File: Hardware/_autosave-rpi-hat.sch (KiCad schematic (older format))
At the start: 2 parts, among them J1 Conn_02x20_Odd_Even__Rpi, J2 USART

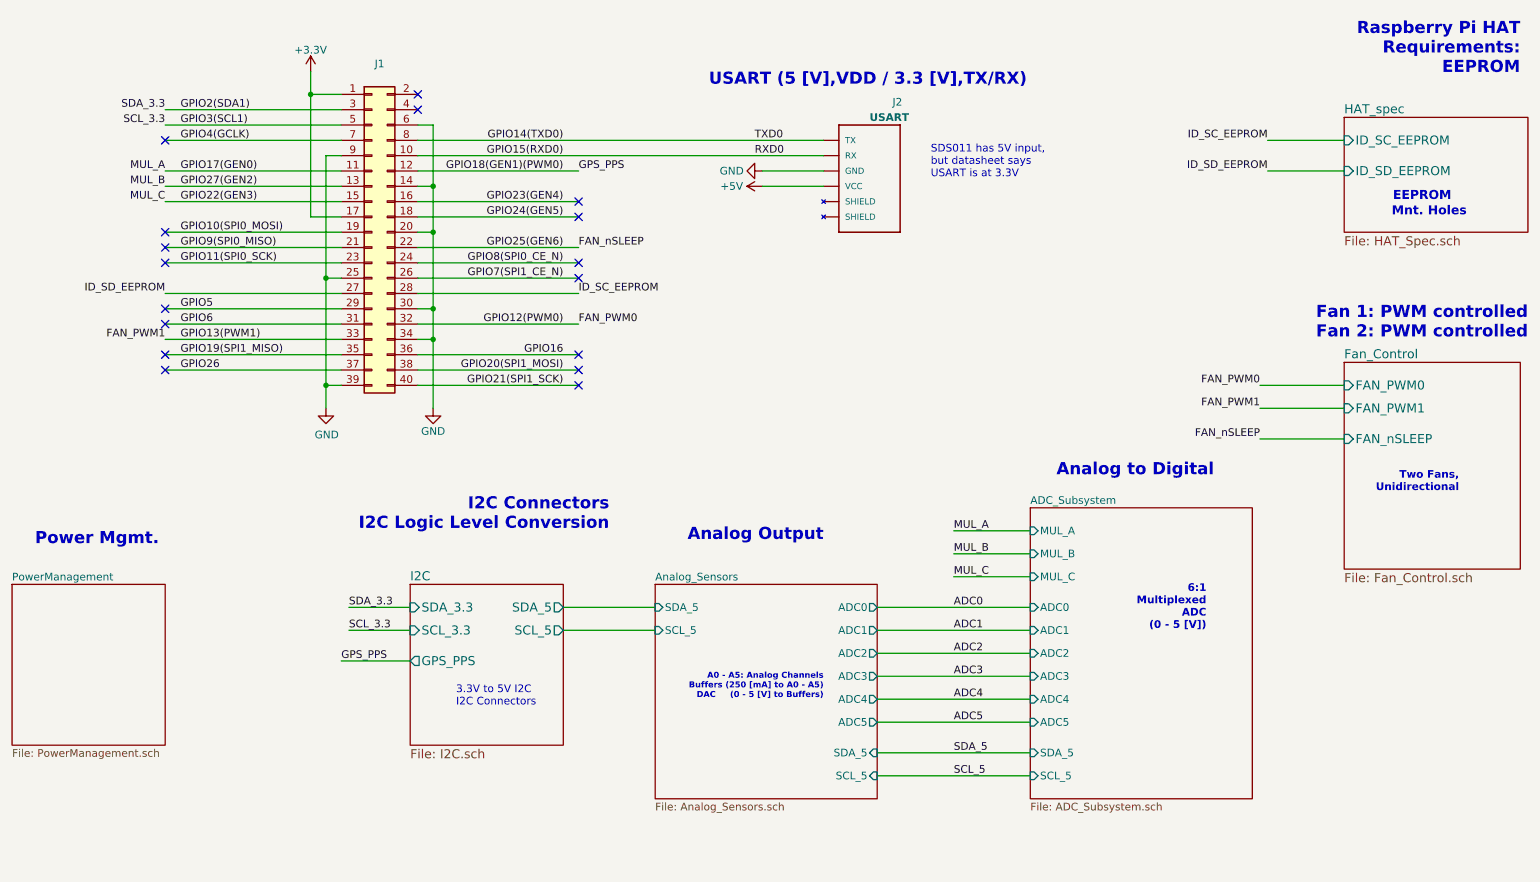
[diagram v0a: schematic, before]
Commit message: Organized Schematic Naming and Added Comments
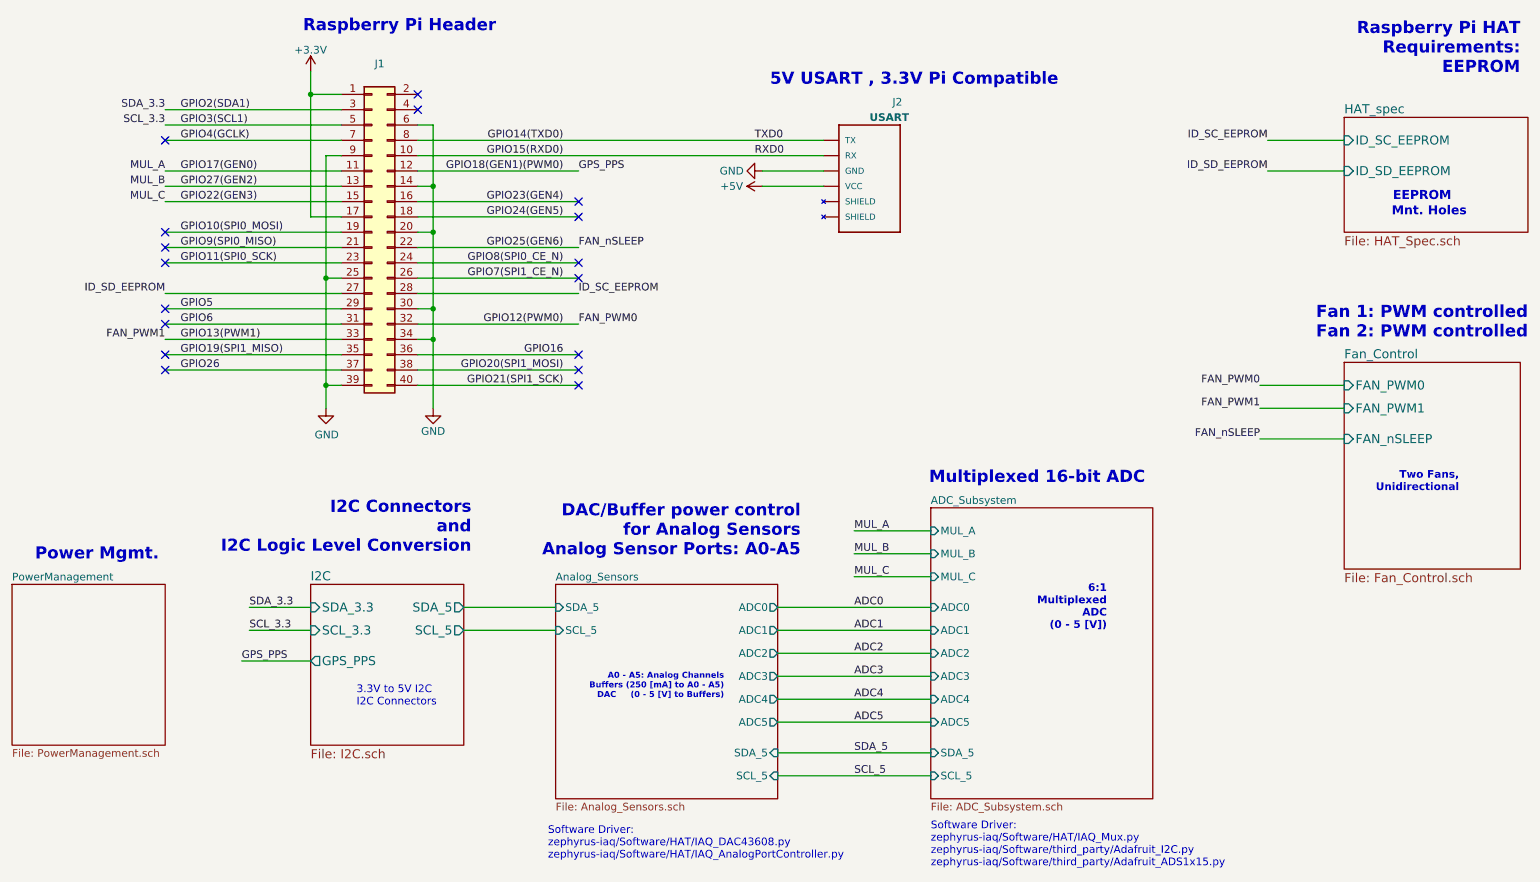
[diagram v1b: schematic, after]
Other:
- note added: "5V USART , 3.3V Pi Compatible"
- note added: "DAC/Buffer power control\n for Analog Sensors\nAnalog Sensor Ports: A0-A5\n\n"
- note added: "I2C Connectors\nand\nI2C Logic Level Conversion"
- note added: "Multiplexed 16-bit ADC"
- note added: "Raspberry Pi Header"
- note added: "Software Driver:\nzephyrus-iaq/Software/HAT/IAQ_DAC43608.py\nzephyrus-iaq/Software/HAT/IAQ_AnalogPortController.py"
- note added: "Software Driver:\nzephyrus-iaq/Software/HAT/IAQ_Mux.py\nzephyrus-iaq/Software/third_party/Adafruit_I2C.py\nzephyrus-iaq/Software/third_party/Adafruit_ADS1x15.py"
- note removed: "Analog Output\n\n"
- note removed: "Analog to Digital"
- note removed: "I2C Connectors\nI2C Logic Level Conversion"
- note removed: "SDS011 has 5V input, \nbut datasheet says \nUSART is at 3.3V"
- note removed: "USART (5 [V],VDD / 3.3 [V],TX/RX)"
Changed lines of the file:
@@
 EESchema Schematic File Version 4
-LIBS:rpi-hat-cache
 EELAYER 30 0
 EELAYER END
@@
 encoding utf-8
 Sheet 1 7
-Title ""
-Date "15 nov 2012"
+Title "IAQ HAT Top Level"
+Date "2019-11-15"
 Rev ""
-Comp ""
+Comp "Zephyrus, Indoor Air Quality - Raspberry Pi HAT"
 Comment1 ""
 Comment2 ""
@@
 	1    0    0    -1
 $EndComp
-Text Notes 5550 1150 0    79   ~ 16
-USART (5 [V],VDD / 3.3 [V],TX/RX)
-Text Label 7150 4550 0    50   ~ 0
+Text Notes 5950 1150 0    79   ~ 16
+5V USART , 3.3V Pi Compatible
+Text Label 6500 4550 0    50   ~ 0
 ADC0
-Text Label 7150 4700 0    50   ~ 0
+Text Label 6500 4700 0    50   ~ 0
 ADC1
-Text Label 7150 4850 0    50   ~ 0
+Text Label 6500 4850 0    50   ~ 0
 ADC2
-Text Label 7150 5000 0    50   ~ 0
+Text Label 6500 5000 0    50   ~ 0
 ADC3
-Text Label 7150 5150 0    50   ~ 0
+Text Label 6500 5150 0    50   ~ 0
 ADC4
-Text Label 7150 5300 0    50   ~ 0
+Text Label 6500 5300 0    50   ~ 0
 ADC5
-Text Label 3200 4550 0    50   ~ 0
+Text Label 2550 4550 0    50   ~ 0
 SDA_3.3
 Text Label 2000 1300 2    50   ~ 0
@@
 	3050 1600 3050 2400
 Connection ~ 3050 2400
-Text Notes 7000 1750 0    50   ~ 0
-SDS011 has 5V input, \nbut datasheet says \nUSART is at 3.3V
 NoConn ~ 4700 2300
 NoConn ~ 2000 2100
@@
 NoConn ~ 2000 2300
 $Sheet
-S 7650 3900 1450 1900
+S 7000 3900 1450 1900
 U 5D9BB3B6
 F0 "ADC_Subsystem" 50
 F1 "ADC_Subsystem.sch" 50
-F2 "ADC0" I L 7650 4550 50
-F3 "ADC1" I L 7650 4700 50
-F4 "ADC2" I L 7650 4850 50
-F5 "ADC3" I L 7650 5000 50
-F6 "ADC4" I L 7650 5150 50
-F7 "ADC5" I L 7650 5300 50
-F8 "MUL_A" I L 7650 4050 50
-F9 "MUL_B" I L 7650 4200 50
-F10 "MUL_C" I L 7650 4350 50
-F11 "SDA_5" I L 7650 5500 50
-F12 "SCL_5" I L 7650 5650 50
-$EndSheet
-Text Label 7150 4050 0    50   ~ 0
+F2 "ADC0" I L 7000 4550 50
+F3 "ADC1" I L 7000 4700 50
+F4 "ADC2" I L 7000 4850 50
+F5 "ADC3" I L 7000 5000 50
+F6 "ADC4" I L 7000 5150 50
+F7 "ADC5" I L 7000 5300 50
+F8 "MUL_A" I L 7000 4050 50
+F9 "MUL_B" I L 7000 4200 50
+F10 "MUL_C" I L 7000 4350 50
+F11 "SDA_5" I L 7000 5500 50
+F12 "SCL_5" I L 7000 5650 50
+$EndSheet
+Text Label 6500 4050 0    50   ~ 0
 MUL_A
 Wire Wire Line
-	7650 4050 7150 4050
-Wire Wire Line
-	7150 4200 7650 4200
-Wire Wire Line
-	7150 4350 7650 4350
-Text Label 7150 5500 0    50   ~ 0
+	7000 4050 6500 4050
+Wire Wire Line
+	6500 4200 7000 4200
+Wire Wire Line
+	6500 4350 7000 4350
+Text Label 6500 5500 0    50   ~ 0
 SDA_5
-Text Label 7150 5650 0    50   ~ 0
+Text Label 6500 5650 0    50   ~ 0
 SCL_5
-Text Label 7150 4200 0    50   ~ 0
+Text Label 6500 4200 0    50   ~ 0
 MUL_B
-Text Label 7150 4350 0    50   ~ 0
+Text Label 6500 4350 0    50   ~ 0
 MUL_C
 Text Label 2000 1700 2    50   ~ 0
@@
 F1 "PowerManagement.sch" 50
 $EndSheet
-Text Label 3200 4700 0    50   ~ 0
+Text Label 2550 4700 0    50   ~ 0
 SCL_3.3
 NoConn ~ 4700 1900
-Text Notes 1150 4150 0    79   ~ 16
+Text Notes 1150 4250 0    79   ~ 16
 Power Mgmt.
-Text Notes 6300 4250 2    79   ~ 16
-Analog Output\n\n
-Text Notes 6300 5150 2    39   ~ 8
+Text Notes 6150 4350 2    79   ~ 16
+DAC/Buffer power control\n for Analog Sensors\nAnalog Sensor Ports: A0-A5\n\n
+Text Notes 5650 5150 2    39   ~ 8
 A0 - A5: Analog Channels\nBuffers (250 [mA] to A0 - A5)\nDAC     (0 - 5 [V] to Buffers)
 $Sheet
@@
 $EndSheet
 Wire Wire Line
-	6650 4550 7650 4550
-Wire Wire Line
-	6650 4700 7650 4700
-Wire Wire Line
-	6650 4850 7650 4850
-Wire Wire Line
-	6650 5000 7650 5000
-Wire Wire Line
-	6650 5150 7650 5150
-Wire Wire Line
-	6650 5300 7650 5300
-$Sheet
-S 3600 4400 1000 1050
+	6000 4550 7000 4550
+Wire Wire Line
+	6000 4700 7000 4700
+Wire Wire Line
+	6000 4850 7000 4850
+Wire Wire Line
+	6000 5000 7000 5000
+Wire Wire Line
+	6000 5150 7000 5150
+Wire Wire Line
+	6000 5300 7000 5300
+$Sheet
+S 2950 4400 1000 1050
 U 5DB861AF
 F0 "I2C" 59
 F1 "I2C.sch" 59
-F2 "SDA_3.3" I L 3600 4550 59
-F3 "SCL_3.3" I L 3600 4700 59
-F4 "SDA_5" O R 4600 4550 59
-F5 "SCL_5" O R 4600 4700 59
-F6 "GPS_PPS" O L 3600 4900 59
-$EndSheet
-Text Label 3150 4900 0    50   ~ 0
+F2 "SDA_3.3" I L 2950 4550 59
+F3 "SCL_3.3" I L 2950 4700 59
+F4 "SDA_5" O R 3950 4550 59
+F5 "SCL_5" O R 3950 4700 59
+F6 "GPS_PPS" O L 2950 4900 59
+$EndSheet
+Text Label 2500 4900 0    50   ~ 0
 GPS_PPS
 NoConn ~ 4700 2000
 Wire Wire Line
-	3600 4900 3150 4900
+	2950 4900 2500 4900
 Wire Wire Line
 	3650 1600 6300 1600
@@
 Text Notes 10450 3800 2    50   ~ 10
 Two Fans, \nUnidirectional
-Text Notes 8800 4700 2    50   ~ 10
+Text Notes 8150 4700 2    50   ~ 10
 6:1\nMultiplexed\nADC\n (0 - 5 [V])
-Text Notes 3900 5200 0    50   ~ 0
+Text Notes 3250 5200 0    50   ~ 0
 3.3V to 5V I2C\nI2C Connectors
-Text Notes 8850 3700 2    79   ~ 16
-Analog to Digital
-Text Notes 4900 4050 2    79   ~ 16
-I2C Connectors\nI2C Logic Level Conversion
+Text Notes 8400 3750 2    79   ~ 16
+Multiplexed 16-bit ADC
+Text Notes 4000 4200 2    79   ~ 16
+I2C Connectors\nand\nI2C Logic Level Conversion
 Text Notes 10900 2800 2    79   ~ 16
 Fan 1: PWM controlled\nFan 2: PWM controlled
@@
 Raspberry Pi HAT\nRequirements:\nEEPROM\n\n
 Wire Wire Line
-	6650 5500 7650 5500
-Wire Wire Line
-	6650 5650 7650 5650
-Wire Wire Line
-	3200 4550 3600 4550
-Wire Wire Line
-	3200 4700 3600 4700
-$Sheet
-S 5200 4400 1450 1400
+	6000 5500 7000 5500
+Wire Wire Line
+	6000 5650 7000 5650
+Wire Wire Line
+	2550 4550 2950 4550
+Wire Wire Line
+	2550 4700 2950 4700
+$Sheet
+S 4550 4400 1450 1400
 U 5DA09389
 F0 "Analog_Sensors" 50
 F1 "Analog_Sensors.sch" 50
-F2 "ADC0" O R 6650 4550 50
-F3 "ADC1" O R 6650 4700 50
-F4 "ADC2" O R 6650 4850 50
-F5 "ADC3" O R 6650 5000 50
-F6 "ADC4" O R 6650 5150 50
-F7 "ADC5" O R 6650 5300 50
-F8 "SDA_5" I L 5200 4550 50
-F9 "SCL_5" I L 5200 4700 50
-F10 "SDA_5" I R 6650 5500 50
-F11 "SCL_5" I R 6650 5650 50
-$EndSheet
-Wire Wire Line
-	4600 4550 5200 4550
-Wire Wire Line
-	4600 4700 5200 4700
+F2 "ADC0" O R 6000 4550 50
+F3 "ADC1" O R 6000 4700 50
+F4 "ADC2" O R 6000 4850 50
+F5 "ADC3" O R 6000 5000 50
+F6 "ADC4" O R 6000 5150 50
+F7 "ADC5" O R 6000 5300 50
+F8 "SDA_5" I L 4550 4550 50
+F9 "SCL_5" I L 4550 4700 50
+F10 "SDA_5" I R 6000 5500 50
+F11 "SCL_5" I R 6000 5650 50
+$EndSheet
+Wire Wire Line
+	3950 4550 4550 4550
+Wire Wire Line
+	3950 4700 4550 4700
+Text Notes 4500 6200 0    50   ~ 0
+Software Driver:\nzephyrus-iaq/Software/HAT/IAQ_DAC43608.py\nzephyrus-iaq/Software/HAT/IAQ_AnalogPortController.py
+Text Notes 7000 6250 0    50   ~ 0
+Software Driver:\nzephyrus-iaq/Software/HAT/IAQ_Mux.py\nzephyrus-iaq/Software/third_party/Adafruit_I2C.py\nzephyrus-iaq/Software/third_party/Adafruit_ADS1x15.py
+Text Notes 2900 800  0    79   ~ 16
+Raspberry Pi Header
 $EndSCHEMATC
